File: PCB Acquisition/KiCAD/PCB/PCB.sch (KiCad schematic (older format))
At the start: 3 parts, among them U1 PIC24F32KA302-I_SS

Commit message: Début du layout
Les pièces ont été choisies pour le PCB et le layout du PCB avec celles-ci est commencé. Il reste à finaliser le layout.
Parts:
- removed U?: Pickit_3, symbol PIC:Pickit_3
- added J1: Conn_01x06_Female, Connector_PinSocket_2.54mm:PinSocket_1x06_P2.54mm_Vertical, symbol Connector:Conn_01x06_Female
- added J2: Conn_01x03_Male, Connector_PinHeader_2.54mm:PinHeader_1x03_P2.54mm_Vertical, symbol Connector:Conn_01x03_Male
- added J3: Conn_01x02_Male, Connector_Molex:Molex_KK-396_A-41791-0002_1x02_P3.96mm_Vertical, symbol Connector:Conn_01x02_Male
- R1: footprint (none) -> Resistor_THT:R_Axial_DIN0207_L6.3mm_D2.5mm_P7.62mm_Horizontal
- U1: symbol 2020-04-10_20-01-39:PIC24F32KA302-I_SS -> PCB-rescue:PIC24F32KA302-I_SS-2020-04-10_20-01-39
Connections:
- wire segments 33 -> 34
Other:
- note added: "Pickit 3"
- note removed: "Communication I2C\navec un autre uC"
- moved on the sheet: R1, U1
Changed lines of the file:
@@
 Comment4 ""
 $EndDescr
+Wire Wire Line
+	1500 2850 2000 2850
+Wire Wire Line
+	1400 2950 2000 2950
+Wire Wire Line
+	1650 3250 2000 3250
+Wire Wire Line
+	1550 3750 2000 3750
 $Comp
-L 2020-04-10_20-01-39:PIC24F32KA302-I_SS U1
+L Device:R R1
+U 1 1 5F6DF8B5
+P 1800 1300
+F 0 "R1" V 1593 1300 50  0000 C CNN
+F 1 "1k" V 1684 1300 50  0000 C CNN
+F 2 "Resistor_THT:R_Axial_DIN0207_L6.3mm_D2.5mm_P7.62mm_Horizontal" V 1730 1300 50  0001 C CNN
+F 3 "~" H 1800 1300 50  0001 C CNN
+	1    1800 1300
+	0    1    1    0
+$EndComp
+Wire Wire Line
+	1600 900  2000 900
+Wire Wire Line
+	2000 3150 1350 3150
+Text Notes 2150 5100 0    50   ~ 0
+SIG ou RAW
+Wire Wire Line
+	1650 3250 1150 3250
+Connection ~ 1650 3250
+Wire Wire Line
+	1550 3750 950  3750
+Wire Wire Line
+	950  3750 950  5300
+Connection ~ 1550 3750
+Text Notes 2150 5200 0    50   ~ 0
+Vss (GND)\n
+Text Notes 2150 5300 0    50   ~ 0
+Vdd
+$Comp
+L Connector:Conn_01x03_Male J2
+U 1 1 6009B195
+P 2050 5200
+F 0 "J2" H 2100 5050 50  0000 R CNN
+F 1 "Conn_01x03_Male" H 2400 4950 50  0000 R CNN
+F 2 "Connector_PinHeader_2.54mm:PinHeader_1x03_P2.54mm_Vertical" H 2050 5200 50  0001 C CNN
+F 3 "~" H 2050 5200 50  0001 C CNN
+	1    2050 5200
+	-1   0    0    -1
+$EndComp
+Wire Wire Line
+	1850 5200 1150 5200
+Wire Wire Line
+	1150 3250 1150 5200
+Wire Wire Line
+	950  5300 1850 5300
+Wire Wire Line
+	1350 5100 1850 5100
+Wire Wire Line
+	1350 3150 1350 5100
+$Comp
+L Connector:Conn_01x06_Female J1
+U 1 1 600A24D0
+P 900 1400
+F 0 "J1" H 792 1785 50  0000 C CNN
+F 1 "Conn_01x06_Female" H 792 1694 50  0000 C CNN
+F 2 "Connector_PinSocket_2.54mm:PinSocket_1x06_P2.54mm_Vertical" H 900 1400 50  0001 C CNN
+F 3 "~" H 900 1400 50  0001 C CNN
+	1    900  1400
+	-1   0    0    -1
+$EndComp
+Wire Wire Line
+	1100 1600 1400 1600
+Wire Wire Line
+	1400 1600 1400 2950
+Wire Wire Line
+	1100 1500 1500 1500
+Wire Wire Line
+	1500 1500 1500 2850
+Wire Wire Line
+	1100 1400 1650 1400
+Wire Wire Line
+	1650 1400 1650 3250
+Wire Wire Line
+	1100 1200 1600 1200
+Wire Wire Line
+	1600 1200 1600 900
+Wire Wire Line
+	1100 1300 1550 1300
+Wire Wire Line
+	2000 900  2000 1300
+Wire Wire Line
+	1950 1300 2000 1300
+Connection ~ 2000 1300
+Wire Wire Line
+	2000 1300 2000 2550
+Wire Wire Line
+	1550 1300 1550 3750
+Connection ~ 1550 1300
+Wire Wire Line
+	1550 1300 1650 1300
+$Comp
+L PCB-rescue:PIC24F32KA302-I_SS-2020-04-10_20-01-39 U1
 U 1 1 5E90D797
 P 2000 2550
@@
 	1    0    0    -1
 $EndComp
+Text Notes 8400 5000 0    50   ~ 0
+SCL\n
+Text Notes 8400 5100 0    50   ~ 0
+SDA
 $Comp
-L PIC:Pickit_3 U?
-U 1 1 5F6DC992
-P 950 1500
-F 0 "U?" H 987 2015 50  0000 C CNN
-F 1 "Pickit_3" H 987 1924 50  0000 C CNN
-F 2 "" H 950 1500 50  0001 C CNN
-F 3 "" H 950 1500 50  0001 C CNN
-	1    950  1500
+L Connector:Conn_01x02_Male J3
+U 1 1 600B67EA
+P 8600 5000
+F 0 "J3" H 8700 5250 50  0000 C CNN
+F 1 "Conn_01x02_Male" H 8700 5150 50  0000 C CNN
+F 2 "Connector_Molex:Molex_KK-396_A-41791-0002_1x02_P3.96mm_Vertical" H 8600 5000 50  0001 C CNN
+F 3 "~" H 8600 5000 50  0001 C CNN
+	1    8600 5000
 	1    0    0    -1
 $EndComp
 Wire Wire Line
-	1300 1550 1500 1550
+	8800 5000 9700 5000
 Wire Wire Line
-	1500 1550 1500 2850
+	9700 5000 9700 3650
 Wire Wire Line
-	1500 2850 2000 2850
+	9700 3650 9500 3650
 Wire Wire Line
-	1300 1650 1400 1650
+	9500 3550 9800 3550
 Wire Wire Line
-	1400 1650 1400 2950
+	9800 3550 9800 5100
 Wire Wire Line
-	1400 2950 2000 2950
-Wire Wire Line
-	1300 1450 1650 1450
-Wire Wire Line
-	1650 1450 1650 3250
-Wire Wire Line
-	1650 3250 2000 3250
-Wire Wire Line
-	1300 1350 1550 1350
-Wire Wire Line
-	1550 1350 1550 3750
-Wire Wire Line
-	1550 3750 2000 3750
-$Comp
-L Device:R R1
-U 1 1 5F6DF8B5
-P 1850 1350
-F 0 "R1" V 1643 1350 50  0000 C CNN
-F 1 "1k" V 1734 1350 50  0000 C CNN
-F 2 "" V 1780 1350 50  0001 C CNN
-F 3 "~" H 1850 1350 50  0001 C CNN
-	1    1850 1350
-	0    1    1    0
-$EndComp
-Wire Wire Line
-	1550 1350 1700 1350
-Connection ~ 1550 1350
-Wire Wire Line
-	1300 1250 1600 1250
-Wire Wire Line
-	1600 1250 1600 900
-Wire Wire Line
-	1600 900  2000 900
-Wire Wire Line
-	2000 900  2000 1350
-Wire Wire Line
-	2000 2550 2000 1350
-Connection ~ 2000 1350
-Wire Wire Line
-	12800 1300 12800 3550
-Wire Wire Line
-	12800 3550 12600 3550
-Wire Wire Line
-	9200 1300 12800 1300
-Wire Wire Line
-	12600 3650 13050 3650
-Wire Wire Line
-	13050 3650 13050 1100
-Wire Wire Line
-	13050 1100 9200 1100
-Text Notes 9750 1000 0    50   ~ 0
-Communication I2C\navec un autre uC
-Text Notes 9200 1050 0    50   ~ 0
-SCL\n
-Text Notes 9200 1250 0    50   ~ 0
-SDA
-Wire Wire Line
-	2000 3150 1350 3150
-Wire Wire Line
-	1350 3150 1350 4900
-Wire Wire Line
-	1350 4900 1650 4900
-Text Notes 1700 4900 0    50   ~ 0
-SIG ou RAW
-Wire Wire Line
-	1650 3250 1150 3250
-Wire Wire Line
-	1150 3250 1150 5150
-Wire Wire Line
-	1150 5150 1650 5150
-Connection ~ 1650 3250
-Wire Wire Line
-	1550 3750 950  3750
-Wire Wire Line
-	950  3750 950  5300
-Wire Wire Line
-	950  5300 1650 5300
-Connection ~ 1550 3750
-Text Notes 1700 5150 0    50   ~ 0
-Vss (GND)\n
-Text Notes 1700 5300 0    50   ~ 0
-Vdd
+	9800 5100 8800 5100
+Text Notes 800  1550 1    50   ~ 0
+Pickit 3
 $EndSCHEMATC

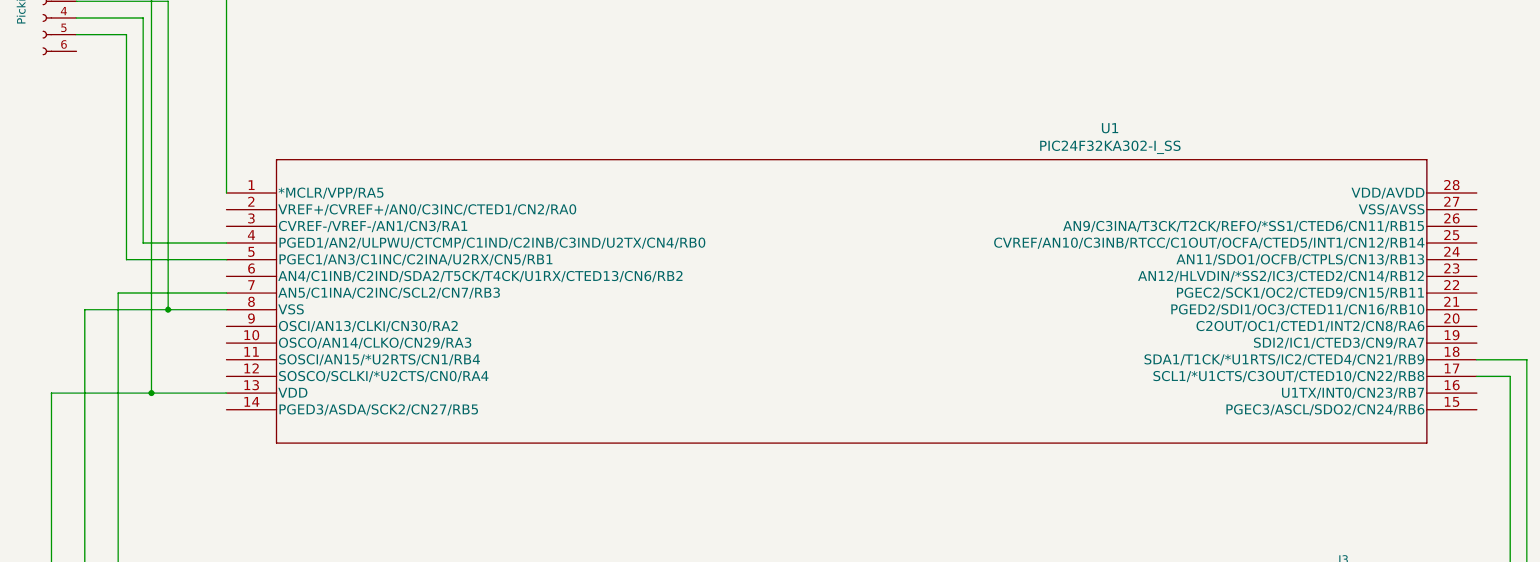
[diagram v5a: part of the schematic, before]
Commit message: Poursuite du layout (tracks)
Les tracks sont finies.
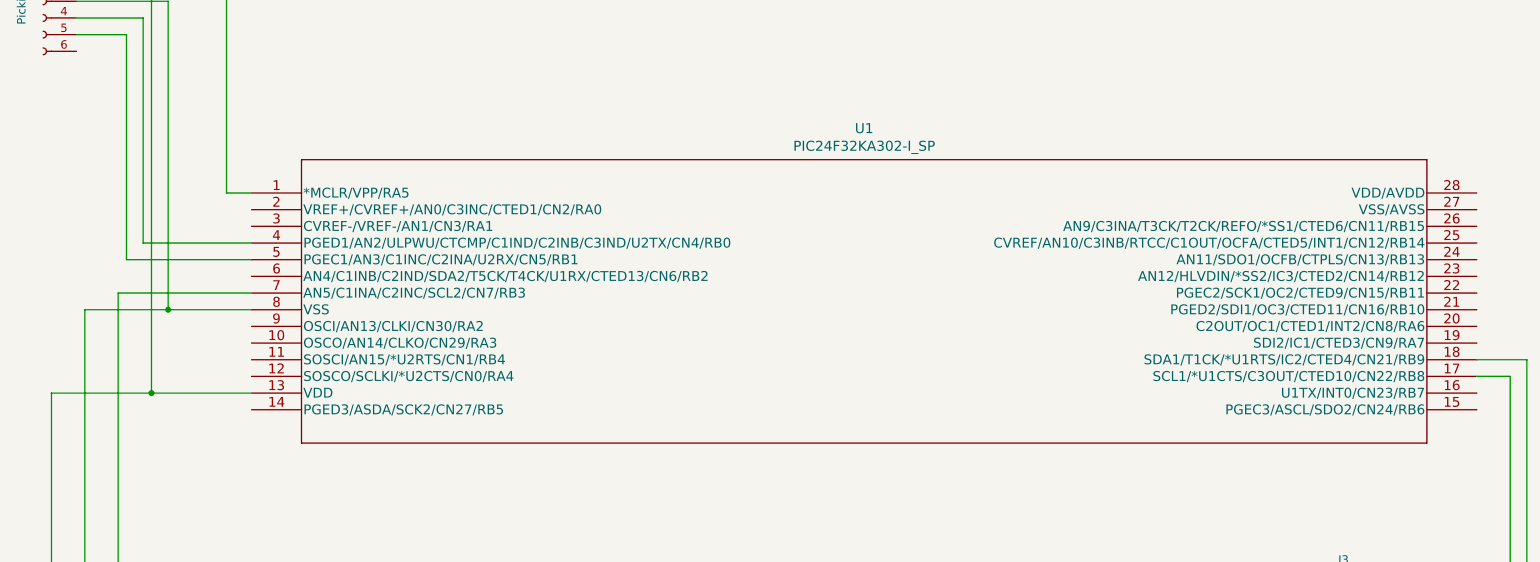
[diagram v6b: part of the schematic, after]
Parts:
- removed U1: PIC24F32KA302-I_SS, 24FV32KA302A:PIC24F32KA302-I&slash_SS, symbol PCB-rescue:PIC24F32KA302-I_SS-2020-04-10_20-01-39
- added U1: PIC24F32KA302-I_SP, PIC24F32KA302:PIC24F32KA302-I&slash_SP, symbol 2021-02-03_15-11-19:PIC24F32KA302-I_SP
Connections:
- net at J1.1 (Pin_1), R1.1: now also U1.1 (*MCLR/VPP/RA5)
- net at J1.2 (Pin_2), J2.3 (Pin_3), R1.2: now also U1.13 (VDD)
- net at J3.1 (Pin_1): now also U1.17 (SCL1/*U1CTS/C3OUT/CTED10/CN22/RB8)
- net at J3.2 (Pin_2): now also U1.18 (SDA1/T1CK/*U1RTS/IC2/CTED4/CN21/RB9)
- net at J1.4 (Pin_4): now also U1.4 (PGED1/AN2/ULPWU/CTCMP/C1IND/C2INB/C3IND/U2TX/CN4/RB0)
- net at J1.5 (Pin_5): now also U1.5 (PGEC1/AN3/C1INC/C2INA/U2RX/CN5/RB1)
- net at J2.1 (Pin_1): now also U1.7 (AN5/C1INA/C2INC/SCL2/CN7/RB3)
- net at J1.3 (Pin_3), J2.2 (Pin_2): now also U1.8 (VSS)
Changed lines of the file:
@@
 Comment4 ""
 $EndDescr
-Wire Wire Line
-	1500 2850 2000 2850
-Wire Wire Line
-	1400 2950 2000 2950
-Wire Wire Line
-	1650 3250 2000 3250
-Wire Wire Line
-	1550 3750 2000 3750
 $Comp
 L Device:R R1
@@
 Wire Wire Line
 	1600 900  2000 900
-Wire Wire Line
-	2000 3150 1350 3150
 Text Notes 2150 5100 0    50   ~ 0
 SIG ou RAW
@@
 Wire Wire Line
 	1550 1300 1650 1300
-$Comp
-L PCB-rescue:PIC24F32KA302-I_SS-2020-04-10_20-01-39 U1
-U 1 1 5E90D797
-P 2000 2550
-F 0 "U1" H 7300 2937 60  0000 C CNN
-F 1 "PIC24F32KA302-I_SS" H 7300 2831 60  0000 C CNN
-F 2 "24FV32KA302A:PIC24F32KA302-I&slash_SS" H 7300 2790 60  0001 C CNN
-F 3 "" H 2000 2550 60  0000 C CNN
-	1    2000 2550
-	1    0    0    -1
-$EndComp
 Text Notes 8400 5000 0    50   ~ 0
 SCL\n
@@
 Text Notes 800  1550 1    50   ~ 0
 Pickit 3
+$Comp
+L 2021-02-03_15-11-19:PIC24F32KA302-I_SP U1
+U 1 1 601AC5B6
+P 2150 2550
+F 0 "U1" H 5825 2937 60  0000 C CNN
+F 1 "PIC24F32KA302-I_SP" H 5825 2831 60  0000 C CNN
+F 2 "PIC24F32KA302:PIC24F32KA302-I&slash_SP" H 7450 2790 60  0001 C CNN
+F 3 "" H 2150 2550 60  0000 C CNN
+	1    2150 2550
+	1    0    0    -1
+$EndComp
+Wire Wire Line
+	1550 3750 2150 3750
+Wire Wire Line
+	1650 3250 2150 3250
+Wire Wire Line
+	1350 3150 2150 3150
+Wire Wire Line
+	1400 2950 2150 2950
+Wire Wire Line
+	1500 2850 2150 2850
+Wire Wire Line
+	2000 2550 2150 2550
 $EndSCHEMATC

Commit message: PCB fini
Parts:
- removed U1: PIC24F32KA302-I_SP, PIC24F32KA302:PIC24F32KA302-I&slash_SP, symbol 2021-02-03_15-11-19:PIC24F32KA302-I_SP
- added J3: ED281DT, digikey-footprints:Socket_DIP-28_7.62mm_Conn, symbol dk_Sockets-for-ICs-Transistors:ED281DT
- J1: value Conn_01x06_Female -> Conn_01x05_Female; symbol Connector:Conn_01x06_Female -> Connector:Conn_01x05_Female
- renumbered J3 to J4
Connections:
- net at J1.1 (Pin_1), R1.1: now also J3.1
- net at J1.2 (Pin_2), J2.3 (Pin_3), R1.2: now also J3.13
- net at J2.1 (Pin_1): now also J3.7
- net at J1.3 (Pin_3), J2.2 (Pin_2): now also J3.8
- net at J1.4 (Pin_4): now also J3.4
- net at J1.5 (Pin_5): now also J3.5
- net at J4.1 (Pin_1): now also J3.18
- net at J4.2 (Pin_2): now also J3.17
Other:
- moved on the sheet: J4
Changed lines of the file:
@@
 	1350 3150 1350 5100
 $Comp
-L Connector:Conn_01x06_Female J1
+L Connector:Conn_01x05_Female J1
 U 1 1 600A24D0
 P 900 1400
 F 0 "J1" H 792 1785 50  0000 C CNN
-F 1 "Conn_01x06_Female" H 792 1694 50  0000 C CNN
+F 1 "Conn_01x05_Female" H 792 1694 50  0000 C CNN
 F 2 "Connector_PinSocket_2.54mm:PinSocket_1x06_P2.54mm_Vertical" H 900 1400 50  0001 C CNN
 F 3 "~" H 900 1400 50  0001 C CNN
@@
 Wire Wire Line
 	1550 1300 1650 1300
-Text Notes 8400 5000 0    50   ~ 0
-SCL\n
-Text Notes 8400 5100 0    50   ~ 0
-SDA
-$Comp
-L Connector:Conn_01x02_Male J3
-U 1 1 600B67EA
-P 8600 5000
-F 0 "J3" H 8700 5250 50  0000 C CNN
-F 1 "Conn_01x02_Male" H 8700 5150 50  0000 C CNN
-F 2 "Connector_Molex:Molex_KK-396_A-41791-0002_1x02_P3.96mm_Vertical" H 8600 5000 50  0001 C CNN
-F 3 "~" H 8600 5000 50  0001 C CNN
-	1    8600 5000
-	1    0    0    -1
-$EndComp
-Wire Wire Line
-	8800 5000 9700 5000
-Wire Wire Line
-	9700 5000 9700 3650
-Wire Wire Line
-	9700 3650 9500 3650
-Wire Wire Line
-	9500 3550 9800 3550
-Wire Wire Line
-	9800 3550 9800 5100
-Wire Wire Line
-	9800 5100 8800 5100
 Text Notes 800  1550 1    50   ~ 0
 Pickit 3
-$Comp
-L 2021-02-03_15-11-19:PIC24F32KA302-I_SP U1
-U 1 1 601AC5B6
-P 2150 2550
-F 0 "U1" H 5825 2937 60  0000 C CNN
-F 1 "PIC24F32KA302-I_SP" H 5825 2831 60  0000 C CNN
-F 2 "PIC24F32KA302:PIC24F32KA302-I&slash_SP" H 7450 2790 60  0001 C CNN
-F 3 "" H 2150 2550 60  0000 C CNN
-	1    2150 2550
-	1    0    0    -1
-$EndComp
 Wire Wire Line
 	1550 3750 2150 3750
@@
 Wire Wire Line
 	2000 2550 2150 2550
+$Comp
+L dk_Sockets-for-ICs-Transistors:ED281DT J3
+U 1 1 6023F95E
+P 2450 3050
+F 0 "J3" H 2400 3775 50  0000 C CNN
+F 1 "ED281DT" H 2400 3684 50  0000 C CNN
+F 2 "digikey-footprints:Socket_DIP-28_7.62mm_Conn" H 2650 3250 60  0001 L CNN
+F 3 "https://media.digikey.com/pdf/Data%20Sheets/On%20Shore%20PDFs/EDXXXDT_Dwg.pdf" H 2650 3350 60  0001 L CNN
+F 4 "ED3050-5-ND" H 2650 3450 60  0001 L CNN "Digi-Key_PN"
+F 5 "ED281DT" H 2650 3550 60  0001 L CNN "MPN"
+F 6 "Connectors, Interconnects" H 2650 3650 60  0001 L CNN "Category"
+F 7 "Sockets for ICs, Transistors" H 2650 3750 60  0001 L CNN "Family"
+F 8 "https://media.digikey.com/pdf/Data%20Sheets/On%20Shore%20PDFs/EDXXXDT_Dwg.pdf" H 2650 3850 60  0001 L CNN "DK_Datasheet_Link"
+F 9 "/product-detail/en/on-shore-technology-inc/ED281DT/ED3050-5-ND/4147600" H 2650 3950 60  0001 L CNN "DK_Detail_Page"
+F 10 "CONN IC DIP SOCKET 28POS TIN" H 2650 4050 60  0001 L CNN "Description"
+F 11 "On Shore Technology Inc." H 2650 4150 60  0001 L CNN "Manufacturer"
+F 12 "Active" H 2650 4250 60  0001 L CNN "Status"
+	1    2450 3050
+	1    0    0    -1
+$EndComp
+Wire Wire Line
+	2650 3650 3650 3650
+Text Notes 4000 3600 2    50   ~ 0
+SDA
+Text Notes 4000 3700 2    50   ~ 0
+SCL\n
+$Comp
+L Connector:Conn_01x02_Male J4
+U 1 1 600B67EA
+P 3850 3550
+F 0 "J4" H 3950 3800 50  0000 C CNN
+F 1 "Conn_01x02_Male" H 3950 3700 50  0000 C CNN
+F 2 "Connector_Molex:Molex_KK-396_A-41791-0002_1x02_P3.96mm_Vertical" H 3850 3550 50  0001 C CNN
+F 3 "~" H 3850 3550 50  0001 C CNN
+	1    3850 3550
+	-1   0    0    -1
+$EndComp
+Wire Wire Line
+	2650 3550 3650 3550
 $EndSCHEMATC
